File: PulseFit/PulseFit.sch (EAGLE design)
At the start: 47 parts, among them SW1 SWITCH.JS202011JCQN

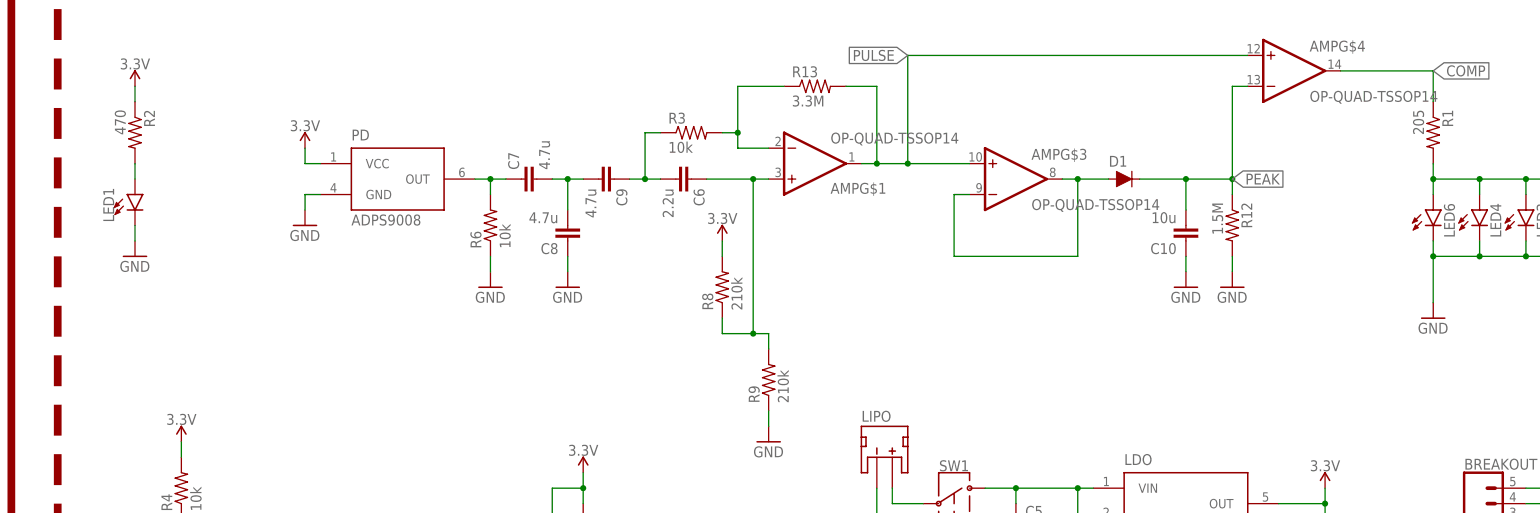
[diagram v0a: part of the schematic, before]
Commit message: reorganized and regrouped repo
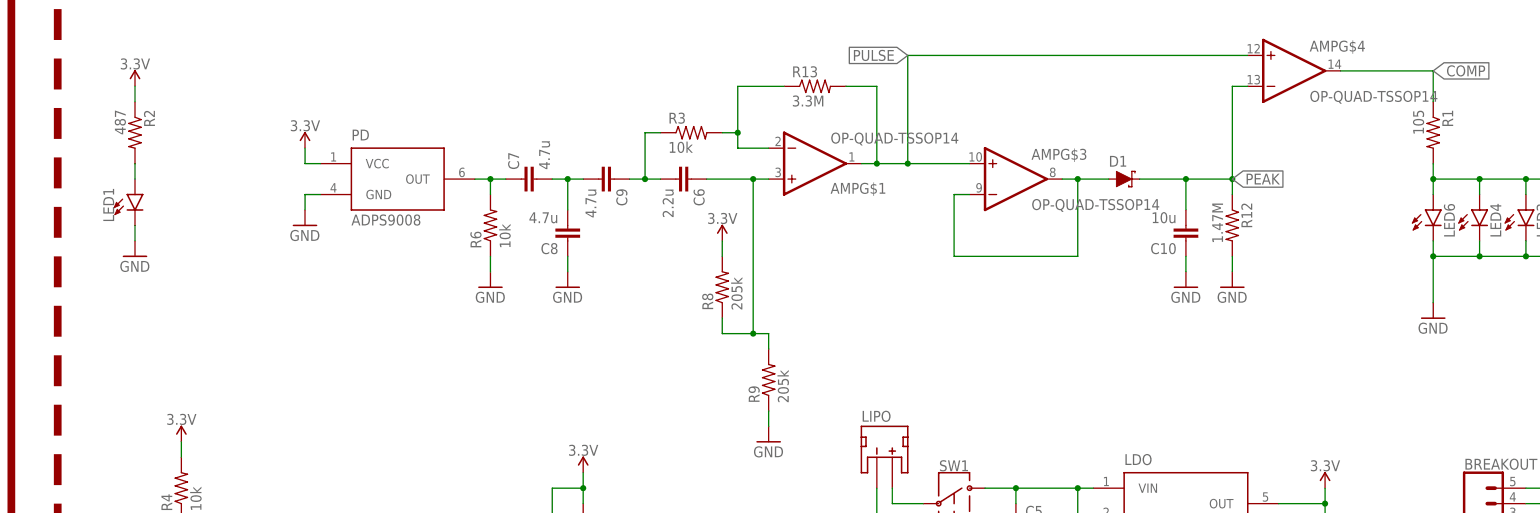
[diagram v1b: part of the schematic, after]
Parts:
- added U$2: REVISION.F, CalvEngIO-Logos:REVISION.F
- D1: device CalvEngIO-DiscreteSemi:DIODE-BAS16J -> CalvEngIO-DiscreteSemi:SCHOTTKY-USC
- R1: value 205 -> 105
- R12: value 1.5M -> 1.47M
- R2: value 470 -> 487
- R8, R9: value 210k -> 205k
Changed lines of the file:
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@@
 <?xml version="1.0" encoding="utf-8"?>
 <!DOCTYPE eagle SYSTEM "eagle.dtd">
-<eagle version="8.2.2">
+<eagle version="8.3.2">
 <drawing>
 <settings>
 <setting alwaysvectorfont="no"/>
+<setting keepoldvectorfont="yes"/>
 <setting verticaltext="up"/>
 </settings>
@@
 <parts>
 <part name="C10" library="CalvEngIO-Passives" deviceset="CAPACITOR" device="0805" value="10u"/>
-<part name="R12" library="CalvEngIO-Passives" deviceset="RESISTOR" device="0402" value="1.5M"/>
+<part name="R12" library="CalvEngIO-Passives" deviceset="RESISTOR" device="0402" value="1.47M"/>
 <part name="GND6" library="SparkFun-Aesthetics" deviceset="GND" device=""/>
 <part name="GND7" library="SparkFun-Aesthetics" deviceset="GND" device=""/>
-<part name="R1" library="CalvEngIO-Passives" deviceset="RESISTOR" device="0402" value="205"/>
+<part name="R1" library="CalvEngIO-Passives" deviceset="RESISTOR" device="0402" value="105"/>
 <part name="GND9" library="SparkFun-Aesthetics" deviceset="GND" device=""/>
 <part name="GND11" library="SparkFun-Aesthetics" deviceset="GND" device=""/>
@@
 <part name="LED19" library="SparkFun-LED" deviceset="LED" device="5MM"/>
 <part name="LED1" library="CalvEngIO-LED" deviceset="LED" device="Z-BEND"/>
-<part name="R2" library="CalvEngIO-Passives" deviceset="RESISTOR" device="0402" value="470"/>
+<part name="R2" library="CalvEngIO-Passives" deviceset="RESISTOR" device="0402" value="487"/>
 <part name="GND15" library="SparkFun-Aesthetics" deviceset="GND" device=""/>
 <part name="LIPO" library="CalvEngIO-Connectors" deviceset="JST_2MM_MALE" device=""/>
@@
 <part name="GND22" library="SparkFun-Aesthetics" deviceset="GND" device=""/>
 <part name="R13" library="CalvEngIO-Passives" deviceset="RESISTOR" device="0402" value="3.3M"/>
-<part name="R8" library="CalvEngIO-Passives" deviceset="RESISTOR" device="0402" value="210k"/>
-<part name="R9" library="CalvEngIO-Passives" deviceset="RESISTOR" device="0402" value="210k"/>
+<part name="R8" library="CalvEngIO-Passives" deviceset="RESISTOR" device="0402" value="205k"/>
+<part name="R9" library="CalvEngIO-Passives" deviceset="RESISTOR" device="0402" value="205k"/>
 <part name="GND23" library="SparkFun-Aesthetics" deviceset="GND" device=""/>
 <part name="R6" library="CalvEngIO-Passives" deviceset="RESISTOR" device="0402" value="10k"/>
@@
 <part name="SW1" library="CalvEngIO-Switches" deviceset="SWITCH.JS202011JCQN" device=""/>
 <part name="GND2" library="SparkFun-Aesthetics" deviceset="GND" device=""/>
-<part name="D1" library="CalvEngIO-DiscreteSemi" deviceset="DIODE" device="-BAS16J"/>
+<part name="D1" library="CalvEngIO-DiscreteSemi" deviceset="SCHOTTKY" device="-USC"/>
 <part name="AMP" library="CalvEngIO-AnalogIC" deviceset="OP-QUAD" device="-TSSOP14" value="OP-QUAD-TSSOP14"/>
 <part name="LDO" library="CalvEngIO-Power" deviceset="AP2210-ADJ" device=""/>
@@
 <part name="SUPPLY7" library="CalvEngIO-Symbols" deviceset="3.3V" device=""/>
 <part name="U$1" library="CalvEngIO-Logos" deviceset="CALVENGIO_HANDLE" device="HANDLE.05" value="CALVENGIO_HANDLEHANDLE.05"/>
+<part name="U$2" library="CalvEngIO-Logos" deviceset="REVISION.F" device=""/>
 </parts>
 <sheets>
@@
 <instance part="SUPPLY7" gate="G$1" x="35.56" y="83.82"/>
 <instance part="U$1" gate="G$1" x="302.26" y="106.68"/>
+<instance part="U$2" gate="G$2" x="76.2" y="127"/>
 </instances>
 <busses>
